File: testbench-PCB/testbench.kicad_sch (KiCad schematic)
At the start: 0 parts

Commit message: Routing the PCB.
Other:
- sheet Kit modules ports: added ENC{A B SW}; removed Encoder_DIO{A B SW}
- sheet MCU ports: added ENC{A B SW}; removed Encoder_DIO{A B SW}
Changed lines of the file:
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@@
     (stroke (width 0) (type default))
   )
-  (bus (pts (xy 148.59 43.815) (xy 191.77 43.815))
+  (bus (pts (xy 148.59 43.18) (xy 191.77 43.18))
     (stroke (width 0) (type default))
   )
@@
     (stroke (width 0) (type default))
   )
-  (wire (pts (xy 148.59 80.645) (xy 191.77 80.645))
+  (wire (pts (xy 148.59 81.28) (xy 191.77 81.28))
     (stroke (width 0) (type default))
   )
@@
     (stroke (width 0) (type default))
   )
-  (bus (pts (xy 148.59 88.265) (xy 191.77 88.265))
+  (bus (pts (xy 148.59 88.9) (xy 191.77 88.9))
     (stroke (width 0) (type default))
   )
@@
     (stroke (width 0) (type default))
   )
-  (bus (pts (xy 148.59 67.945) (xy 191.77 67.945))
+  (bus (pts (xy 148.59 68.58) (xy 191.77 68.58))
     (stroke (width 0) (type default))
   )
@@
       (effects (font (size 1.27 1.27)) (justify right))
     )
-    (pin "{I2C}" bidirectional (at 148.59 43.815 0)
+    (pin "{I2C}" bidirectional (at 148.59 43.18 0)
       (effects (font (size 1.27 1.27)) (justify right))
     )
-    (pin "{RELAY_IO}" bidirectional (at 148.59 67.945 0)
+    (pin "{RELAY_IO}" bidirectional (at 148.59 68.58 0)
       (effects (font (size 1.27 1.27)) (justify right))
     )
-    (pin "RTC_SQW" input (at 148.59 80.645 0)
+    (pin "RTC_SQW" input (at 148.59 81.28 0)
       (effects (font (size 1.27 1.27)) (justify right))
     )
@@
       (effects (font (size 1.27 1.27)) (justify right))
     )
-    (pin "Encoder_DIO{A B SW}" input (at 148.59 88.265 0)
-      (effects (font (size 1.27 1.27)) (justify right))
-    )
     (pin "Speaker_OUT" output (at 148.59 27.94 0)
       (effects (font (size 1.27 1.27)) (justify right))
     )
     (pin "DUT_D[0..20]" bidirectional (at 148.59 97.79 0)
+      (effects (font (size 1.27 1.27)) (justify right))
+    )
+    (pin "ENC{A B SW}" input (at 148.59 88.9 0)
       (effects (font (size 1.27 1.27)) (justify right))
     )
@@
       (effects (font (size 1.27 1.27)) (justify left))
     )
-    (pin "{RELAY_IO}" bidirectional (at 191.77 67.945 180)
+    (pin "{RELAY_IO}" bidirectional (at 191.77 68.58 180)
       (effects (font (size 1.27 1.27)) (justify left))
     )
-    (pin "{I2C}" bidirectional (at 191.77 43.815 180)
+    (pin "{I2C}" bidirectional (at 191.77 43.18 180)
       (effects (font (size 1.27 1.27)) (justify left))
     )
-    (pin "RTC_SQW" output (at 191.77 80.645 180)
-      (effects (font (size 1.27 1.27)) (justify left))
-    )
-    (pin "Encoder_DIO{A B SW}" output (at 191.77 88.265 180)
+    (pin "RTC_SQW" output (at 191.77 81.28 180)
       (effects (font (size 1.27 1.27)) (justify left))
     )
@@
       (effects (font (size 1.27 1.27)) (justify left))
     )
+    (pin "ENC{A B SW}" output (at 191.77 88.9 180)
+      (effects (font (size 1.27 1.27)) (justify left))
+    )

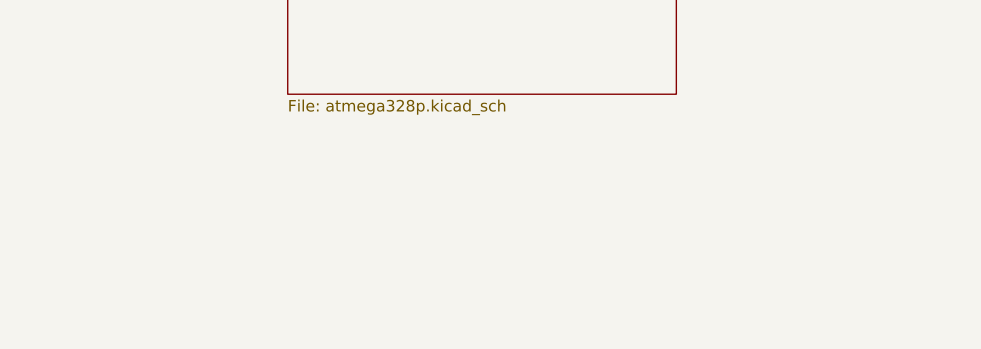
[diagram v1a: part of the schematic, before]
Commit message: Added titles to schematics.
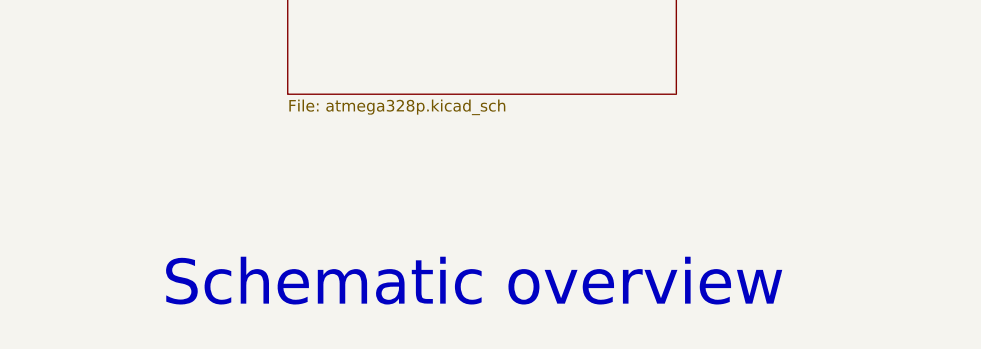
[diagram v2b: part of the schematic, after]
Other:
- note added: "Schematic overview"
- company: (none) -> Company: VUT Brno
- title: (none) -> Test benches for microcontroller kits
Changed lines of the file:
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@@
 (kicad_sch (version 20230121) (generator eeschema)
   (paper "A4")
+  (title_block
+    (title "Test benches for microcontroller kits")
+    (date "2023")
+    (rev "v0.1")
+    (company "Company: VUT Brno")
+    (comment 1 "Author: Ivo Zaludek")
+  )
   (wire (pts (xy 191.77 74.93) (xy 148.59 74.93))
     (stroke (width 0) (type default))
@@
     (stroke (width 0) (type default))
   )
+  (text "Schematic overview" (at 177.8 173.99 0)
+    (effects (font (size 5 5)) (justify left bottom))
+  )
   (sheet (at 97.79 24.13) (size 50.8 80.01) (fields_autoplaced)
